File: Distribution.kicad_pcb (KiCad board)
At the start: 2 copper layers, 6 parts

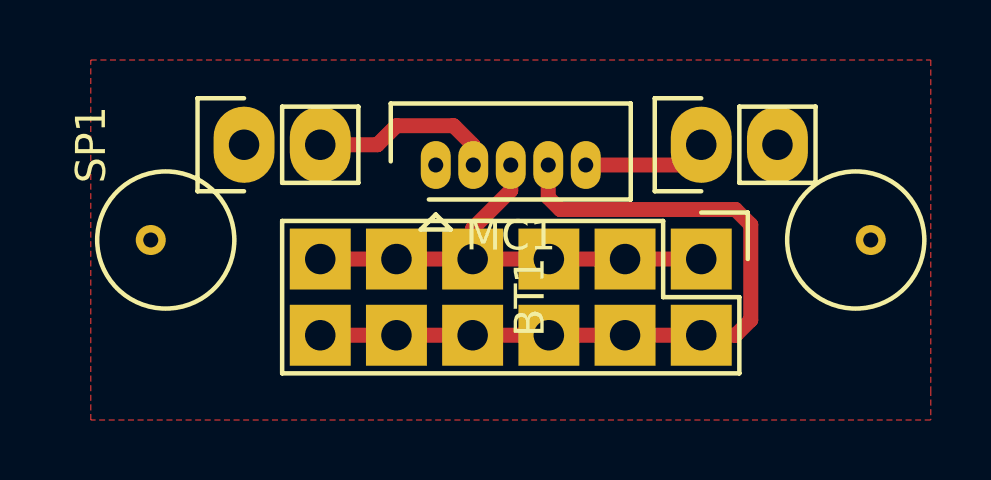
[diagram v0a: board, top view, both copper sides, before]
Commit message: Updated for 2-layer board and added Elecrow files
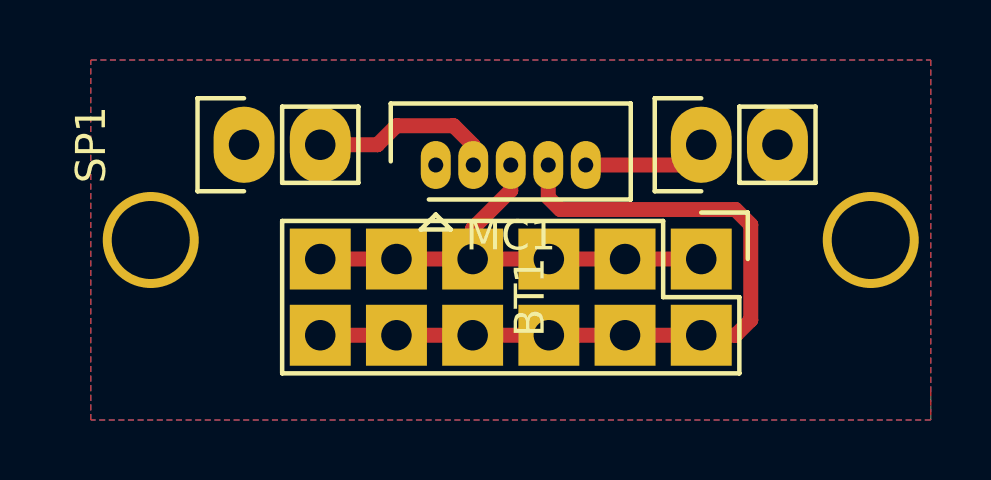
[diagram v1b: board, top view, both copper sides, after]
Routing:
- added copper zone on B.Cu, net GND
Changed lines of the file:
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@@
-(kicad_pcb (version 4) (host pcbnew 4.0.2+dfsg1-stable)
+(kicad_pcb (version 4) (host pcbnew 4.0.7-e2-6376~58~ubuntu16.04.1)
   (general
     (links 16)
     (no_connects 0)
-    (area 134.745 94.09 163.921001 106.965001)
+    (area 134.895 94.24 163.860001 106.965001)
     (thickness 1.6)
     (drawings 0)
@@
   )
   (setup
-    (last_trace_width 0.25)
+    (last_trace_width 0.5)
     (user_trace_width 0.5)
     (trace_clearance 0.2)
@@
     (mod_text_size 1 1)
     (mod_text_width 0.15)
-    (pad_size 1 1)
-    (pad_drill 0.5)
+    (pad_size 3.2 3.2)
+    (pad_drill 2.6)
     (pad_to_mask_clearance 0.2)
     (aux_axis_origin 149.86 100.965)
@@
     (visible_elements FFFEFF7F)
     (pcbplotparams
-      (layerselection 0x00000_00000001)
-      (usegerberextensions false)
+      (layerselection 0x010f0_80000001)
+      (usegerberextensions true)
       (excludeedgelayer false)
       (linewidth 0.100000)
@@
       (padsonsilk false)
       (subtractmaskfromsilk false)
-      (outputformat 5)
-      (mirror true)
-      (drillshape 1)
+      (outputformat 1)
+      (mirror false)
+      (drillshape 0)
       (scaleselection 1)
-      (outputdirectory ""))
+      (outputdirectory ElecrowFiles/))
   )
   (net 0 "")
@@
       (effects (font (size 1 1) (thickness 0.15)))
     )
-    (fp_circle (center 0 0) (end 0 -2.286) (layer F.SilkS) (width 0.15))
-    (pad 1 thru_hole circle (at -0.5 0) (size 1 1) (drill 0.5) (layers *.Cu *.Mask F.SilkS))
+    (pad "" np_thru_hole circle (at -0.5 0) (size 3.2 3.2) (drill 2.6) (layers *.Cu *.Mask))
   )
   (module Connect:1pin (layer F.Cu)
@@
       (effects (font (size 1 1) (thickness 0.15)))
     )
-    (fp_circle (center 0 0) (end 0 -2.286) (layer F.SilkS) (width 0.15))
-    (pad 1 thru_hole circle (at 0.5 0) (size 1 1) (drill 0.5) (layers *.Cu *.Mask F.SilkS))
+    (pad "" np_thru_hole circle (at 0.5 0) (size 3.2 3.2) (drill 2.6) (layers *.Cu *.Mask))
   )
   (module Connectors_Molex:Molex_PicoBlade_53047-0510 (layer F.Cu)
@@
     )
   )
+  (segment (start 156.21 101.6) (end 153.67 101.6) (width 0.5) (layer F.Cu) (net 1))
   (segment (start 148.59 101.6) (end 148.59 100.584) (width 0.5) (layer F.Cu) (net 1))
   (segment (start 148.59 100.584) (end 149.86 99.314) (width 0.5) (layer F.Cu) (net 1))
   (segment (start 149.86 99.314) (end 149.86 98.465) (width 0.5) (layer F.Cu) (net 1))
-  (segment (start 156.21 101.6) (end 153.67 101.6) (width 0.5) (layer F.Cu) (net 1))
   (segment (start 153.67 101.6) (end 151.13 101.6) (width 0.5) (layer F.Cu) (net 1))
   (segment (start 151.13 101.6) (end 148.59 101.6) (width 0.5) (layer F.Cu) (net 1))
@@
   (segment (start 155.535 98.465) (end 156.21 97.79) (width 0.5) (layer F.Cu) (net 3))
   (segment (start 151.11 98.465) (end 151.11 99.548) (width 0.5) (layer F.Cu) (net 5))
+  (segment (start 151.11 99.548) (end 151.511 99.949) (width 0.5) (layer F.Cu) (net 5))
+  (segment (start 151.511 99.949) (end 157.353 99.949) (width 0.5) (layer F.Cu) (net 5))
+  (segment (start 157.353 99.949) (end 157.861 100.457) (width 0.5) (layer F.Cu) (net 5))
+  (segment (start 157.861 100.457) (end 157.861 103.632) (width 0.5) (layer F.Cu) (net 5))
+  (segment (start 157.861 103.632) (end 157.353 104.14) (width 0.5) (layer F.Cu) (net 5))
   (segment (start 157.353 104.14) (end 156.21 104.14) (width 0.5) (layer F.Cu) (net 5))
-  (segment (start 157.861 103.632) (end 157.353 104.14) (width 0.5) (layer F.Cu) (net 5))
-  (segment (start 157.861 100.457) (end 157.861 103.632) (width 0.5) (layer F.Cu) (net 5))
-  (segment (start 157.353 99.949) (end 157.861 100.457) (width 0.5) (layer F.Cu) (net 5))
-  (segment (start 151.511 99.949) (end 157.353 99.949) (width 0.5) (layer F.Cu) (net 5))
-  (segment (start 151.11 99.548) (end 151.511 99.949) (width 0.5) (layer F.Cu) (net 5))
+  (segment (start 146.05 104.14) (end 143.51 104.14) (width 0.5) (layer F.Cu) (net 5))
   (segment (start 157.099 104.14) (end 156.21 104.14) (width 0.5) (layer F.Cu) (net 5))
   (segment (start 156.21 104.14) (end 153.67 104.14) (width 0.5) (layer F.Cu) (net 5))
@@
   (segment (start 151.13 104.14) (end 148.59 104.14) (width 0.5) (layer F.Cu) (net 5))
   (segment (start 148.59 104.14) (end 146.05 104.14) (width 0.5) (layer F.Cu) (net 5))
-  (segment (start 146.05 104.14) (end 143.51 104.14) (width 0.5) (layer F.Cu) (net 5))
   (segment (start 156.21 104.14) (end 156.845 104.14) (width 0.5) (layer F.Cu) (net 5))
   (zone (net 4) (net_name GND) (layer F.Cu) (hatch edge 0.508)
@@
       )
     )
+  )
+  (zone (net 4) (net_name GND) (layer B.Cu) (hatch edge 0.508)
+    (connect_pads (clearance 0.508))
+    (min_thickness 0.254)
+    (fill yes (arc_segments 16) (thermal_gap 0.508) (thermal_bridge_width 0.508))
+    (polygon
+      (pts
+        (xy 163.86 106.965) (xy 135.86 106.965) (xy 135.86 94.965) (xy 163.86 94.965)
+      )
+    )
